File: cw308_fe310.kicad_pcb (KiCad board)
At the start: 2 copper layers, 56 x 67 mm, 22 parts, among them J1 CW308T_CONNBOARD, J2 SerialSel, U1 IS25LP128, U2 SN74LVC1G07DBVR, U3 SN74LVC1G07DBVR, U4 FE310-G000

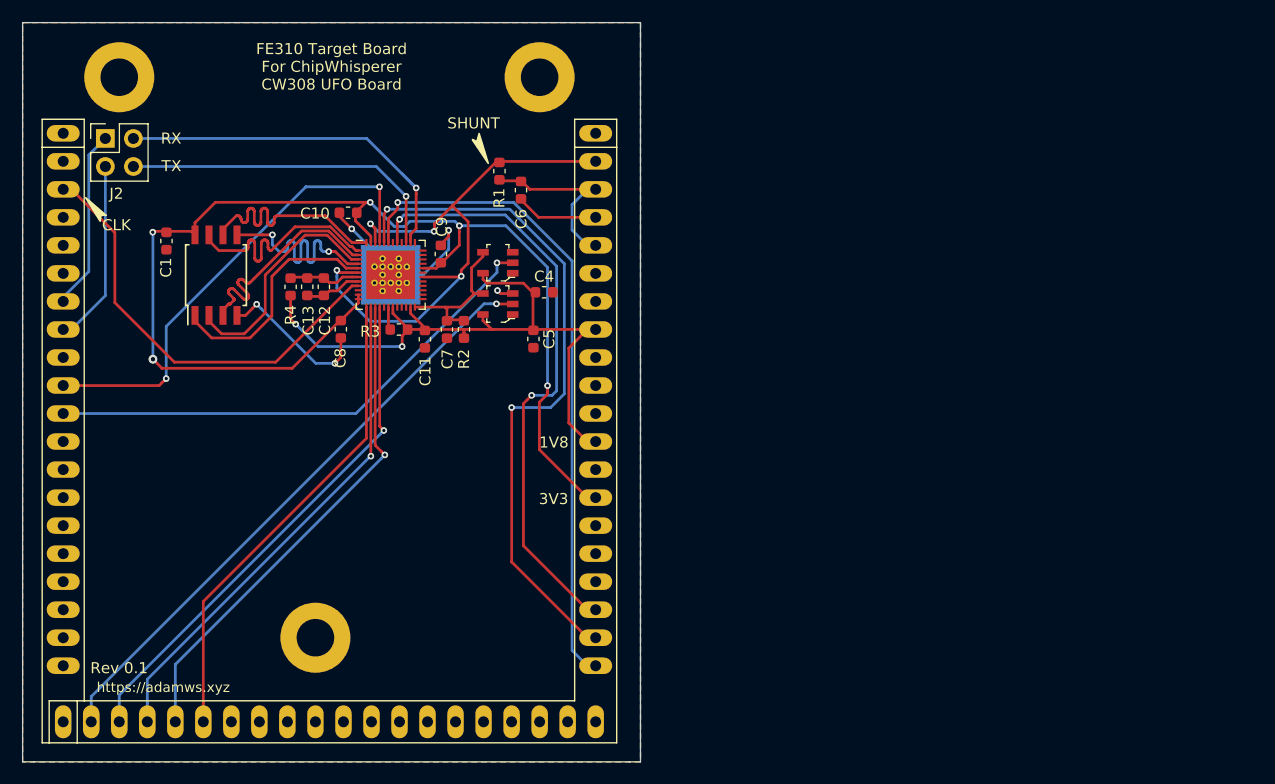
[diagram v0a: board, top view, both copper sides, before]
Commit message: initial commit for revision 0.2 (ftdi added)
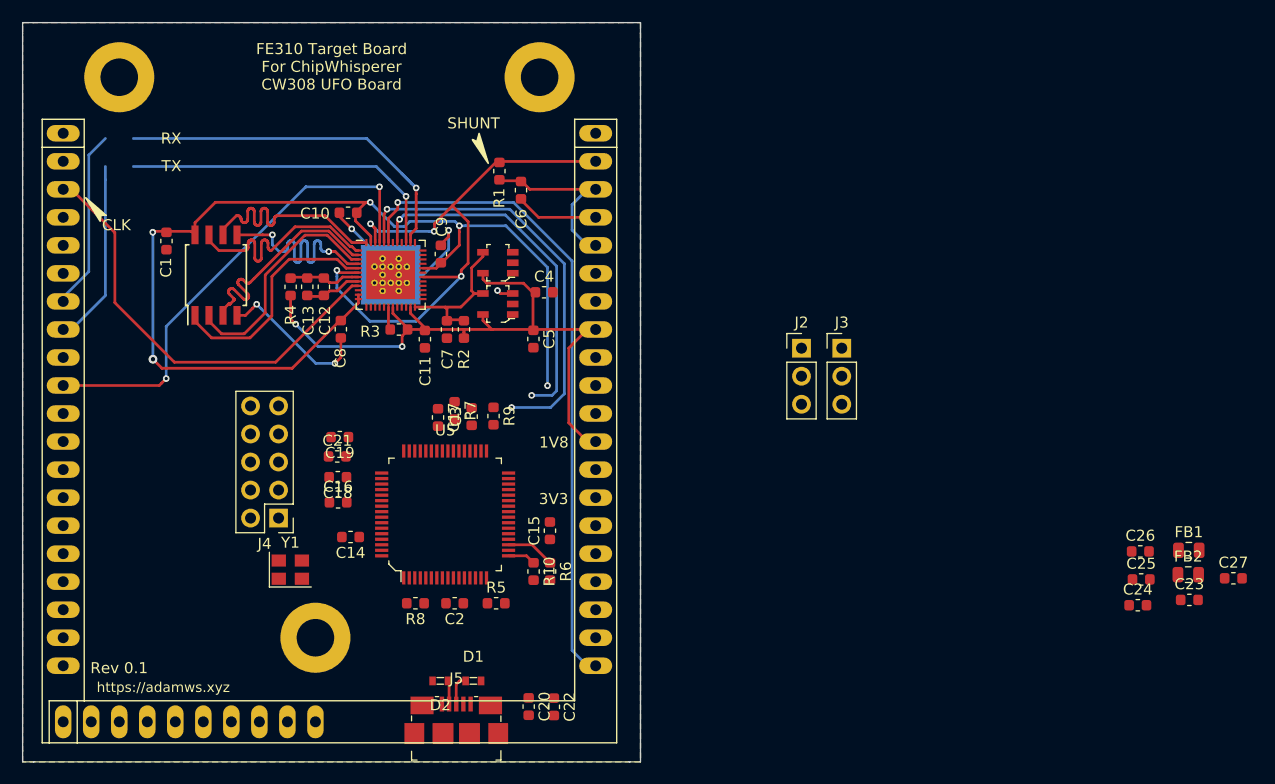
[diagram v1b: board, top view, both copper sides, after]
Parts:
- added C14: 0.1uF, Capacitor_SMD:C_0603_1608Metric, F.Cu at (147.7, 103.6)
- added C15: 0.1uF, Capacitor_SMD:C_0603_1608Metric, F.Cu at (165.8, 103.0)
- added C16: 0.1uF, Capacitor_SMD:C_0603_1608Metric, F.Cu at (146.6, 100.5)
- added C17: 0.1uF, Capacitor_SMD:C_0603_1608Metric, F.Cu at (155.7, 92.8)
- added C18: 0.1uF, Capacitor_SMD:C_0603_1608Metric, F.Cu at (146.6, 98.2)
- added C19: 0.1uF, Capacitor_SMD:C_0603_1608Metric, F.Cu at (146.7, 94.6)
- added C2: 0.1uF, Capacitor_SMD:C_0603_1608Metric, F.Cu at (157.2, 109.6)
- added C20: 0.1uF, Capacitor_SMD:C_0603_1608Metric, F.Cu at (163.9, 119.0)
- added C21: 4.7uF, Capacitor_SMD:C_0603_1608Metric, F.Cu at (146.5, 96.3)
- added C22: 0.1uF, Capacitor_SMD:C_0603_1608Metric, F.Cu at (166.2, 119.0)
- added C23: 0.1uF, Capacitor_SMD:C_0603_1608Metric, F.Cu at (223.7, 109.3)
- added C24: 0.1uF, Capacitor_SMD:C_0603_1608Metric, F.Cu at (219.1, 109.8)
- added C25: 0.1uF, Capacitor_SMD:C_0603_1608Metric, F.Cu at (219.4, 107.5)
- added C26: 4.7uF, Capacitor_SMD:C_0603_1608Metric, F.Cu at (219.3, 104.9)
- added C27: 4.7uF, Capacitor_SMD:C_0603_1608Metric, F.Cu at (227.7, 107.4)
- added C3: 0.1uF, Capacitor_SMD:C_0603_1608Metric, F.Cu at (158.7, 92.7)
- added D1: PGB1010603MR, digikey-footprints:0603, F.Cu at (158.9, 116.7)
- added D2: PGB1010603MR, digikey-footprints:0603, F.Cu at (155.9, 116.7)
- added FB1: Ferrite_Bead, Inductor_SMD:L_0805_2012Metric, F.Cu at (223.7, 104.8)
- added FB2: Ferrite_Bead, Inductor_SMD:L_0805_2012Metric, F.Cu at (223.6, 107.0)
- added J3: Conn_01x03, Connector_PinHeader_2.54mm:PinHeader_1x03_P2.54mm_Vertical, F.Cu at (192.2, 86.5)
- added J4: Conn_02x05_Odd_Even, Connector_PinHeader_2.54mm:PinHeader_2x05_P2.54mm_Vertical, F.Cu at (141.2, 101.9)
- added J5: 10118192-0001LF, digikey-footprints:USB_Micro_B_Female_10118192, F.Cu at (157.3, 121.4)
- added R10: 1K, Resistor_SMD:R_0603_1608Metric, F.Cu at (164.3, 106.7)
- added R5: 1K, Resistor_SMD:R_0603_1608Metric, F.Cu at (160.9, 109.6)
- added R6: 1K, Resistor_SMD:R_0603_1608Metric, F.Cu at (165.8, 106.7)
- added R7: 1K, Resistor_SMD:R_0603_1608Metric, F.Cu at (157.1, 92.2)
- added R8: 12K, Resistor_SMD:R_0603_1608Metric, F.Cu at (153.6, 109.6)
- added R9: 1K, Resistor_SMD:R_0603_1608Metric, F.Cu at (160.7, 92.7)
- added U5: FT2232HL-REEL, digikey-footprints:LQFP-64_10x10mm, F.Cu at (156.3, 101.6)
- added Y1: 12MHz, Oscillator:Oscillator_SMD_Abracon_ASE-4Pin_3.2x2.5mm, F.Cu at (142.3, 106.6)
- J1: footprint CW308T_CONNBOARD -> chipwhisperer:CW308T_CONNBOARD
- J2: value SerialSel -> Conn_01x03; footprint Connector_PinHeader_2.54mm:PinHeader_2x02_P2.54mm_Vertical -> Connector_PinHeader_2.54mm:PinHeader_1x03_P2.54mm_Vertical
- moved J2 65.9 mm to (188.6, 86.5)
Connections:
- J1 pad A20: Net-(J1-PadA20) -> +3V3
- J1 pad B7: Net-(J1-PadB7) -> +3V3
- J2 pad 3: GPIO2 -> FT_TX
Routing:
- net JTAG_TRST: track 55.2 -> 0.00 mm, vias 1 -> 0
- net JTAG_TDI: track 47.7 -> 0.00 mm, vias 1 -> 0
- net UFO.RST: track 46.9 -> 0.00 mm, vias 1 -> 0
- net JTAG_TDO: track 46.0 -> 0.00 mm, vias 1 -> 0
- net JTAG_TMS: track 45.8 -> 0.00 mm, vias 1 -> 0
- net JTAG_TCK: track 43.7 -> 0.00 mm
- net LED2: track 62.8 -> 39.0 mm
- net LED1: track 55.1 -> 33.0 mm
- net +3V3: track 109.0 -> 96.7 mm
- net FT_JTAG_TMS: track 0.00 -> 4.44 mm
- net DP: track 0.00 -> 2.77 mm
- net FT_JTAG_TDI: track 0.00 -> 2.53 mm
- net DM: track 0.00 -> 2.14 mm
